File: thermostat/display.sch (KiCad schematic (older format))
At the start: 20 parts

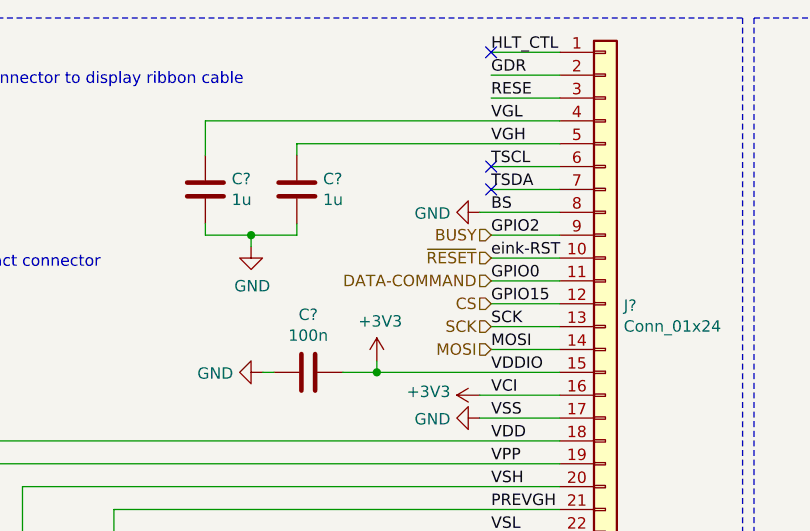
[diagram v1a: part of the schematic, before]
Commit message: Added some comments to pin usage on MKW41Z, reconfigured display to use 3 line SPI (no Data/Command pin) with 9 bit data packets
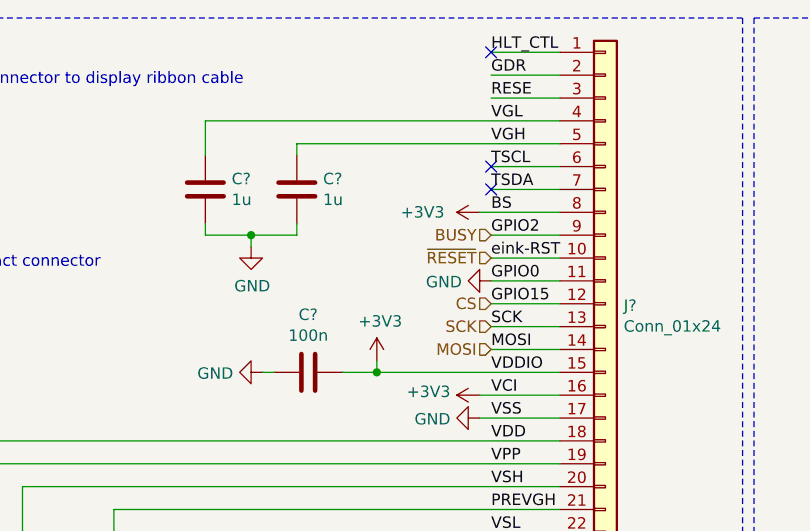
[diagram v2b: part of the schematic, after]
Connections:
- net DATA-COMMAND is gone; now on net GND: J?.11 (Pin_11)
- net +3V3: now also J?.8 (Pin_8)
- net GND: no longer J?.8 (Pin_8)
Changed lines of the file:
@@
 Wire Wire Line
 	5500 3150 5800 3150
-$Comp
-L power:GND #PWR?
-U 1 1 5F315333
-P 5450 3050
-AR Path="/5E63CFCA/5F315333" Ref="#PWR?"  Part="1"
-AR Path="/5F315333" Ref="#PWR?"  Part="1"
-AR Path="/5F306ECC/5F315333" Ref="#PWR?"  Part="1"
-F 0 "#PWR?" H 5450 2800 50  0001 C CNN
-F 1 "GND" V 5455 2922 50  0000 R CNN
-F 2 "" H 5450 3050 50  0001 C CNN
-F 3 "" H 5450 3050 50  0001 C CNN
-	1    5450 3050
-	0    1    1    0
-$EndComp
 Wire Wire Line
 	5450 3050 5800 3050
@@
 Text HLabel 5500 3250 0    50   Input ~ 0
 ~RESET
-Text HLabel 5500 3350 0    50   Input ~ 0
-DATA-COMMAND
 Text HLabel 5500 3450 0    50   Input ~ 0
 CS
+$Comp
+L power:+3V3 #PWR?
+U 1 1 5F5C2508
+P 5450 3050
+AR Path="/5E63CFCA/5F5C2508" Ref="#PWR?"  Part="1"
+AR Path="/5F5C2508" Ref="#PWR?"  Part="1"
+AR Path="/5F306ECC/5F5C2508" Ref="#PWR?"  Part="1"
+F 0 "#PWR?" H 5450 2900 50  0001 C CNN
+F 1 "+3V3" V 5450 3300 50  0000 C CNN
+F 2 "" H 5450 3050 50  0001 C CNN
+F 3 "" H 5450 3050 50  0001 C CNN
+	1    5450 3050
+	0    -1   -1   0
+$EndComp
+$Comp
+L power:GND #PWR?
+U 1 1 5F5C31E6
+P 5500 3350
+AR Path="/5E63CFCA/5F5C31E6" Ref="#PWR?"  Part="1"
+AR Path="/5F5C31E6" Ref="#PWR?"  Part="1"
+AR Path="/5F306ECC/5F5C31E6" Ref="#PWR?"  Part="1"
+F 0 "#PWR?" H 5500 3100 50  0001 C CNN
+F 1 "GND" V 5505 3222 50  0000 R CNN
+F 2 "" H 5500 3350 50  0001 C CNN
+F 3 "" H 5500 3350 50  0001 C CNN
+	1    5500 3350
+	0    1    1    0
+$EndComp
 $EndSCHEMATC

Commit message: Updated symbols after library update, some footprints still need to be assigned. Deleted PCB except for Display and buttons. Button arrangement wrong. Move buttons to other side of Display. Maybe put buttons on separate PCB and create one PCB for MCU and logic, since that needs to be a four layer one. That is expensive and should be kept as small as possible.
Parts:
- L3: renamed from L?; symbol Device:L_Core_Iron -> Device:L_Iron
- gave numbers to parts that had none: 19

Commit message: Replaced DCDC input cap as the package was way too small for the required capacitance, started working on the BOM and looking up parts on Mouser. Need to replace input Molex connector as it is not in stock at Mouser. Easiest is solder pads (I will have a connector on the other side of the cable anyway...) or just the same connector but with higher pincount that Mouser has in stock
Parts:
- L3: symbol Device:L_Iron -> Device:L
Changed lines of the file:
@@
 	7000 3550 7000 3500
 $Comp
-L Device:L_Iron L?
+L Device:L L?
 U 1 1 5F31538B
 P 7450 3500
